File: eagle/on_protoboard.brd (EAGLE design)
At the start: 100 x 80 mm, 15 parts, among them IC2 7812T, K1 G6AK-434P

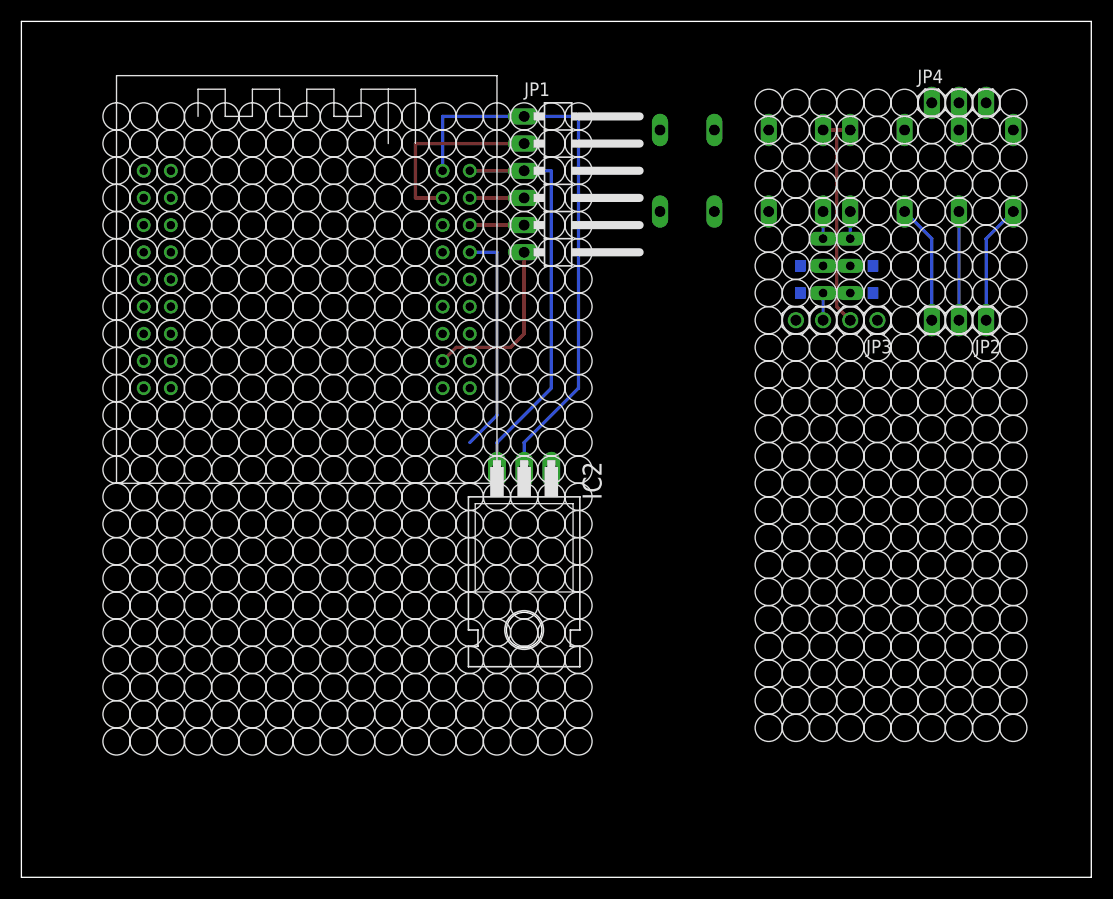
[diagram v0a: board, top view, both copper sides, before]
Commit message: Add digital pulse output device
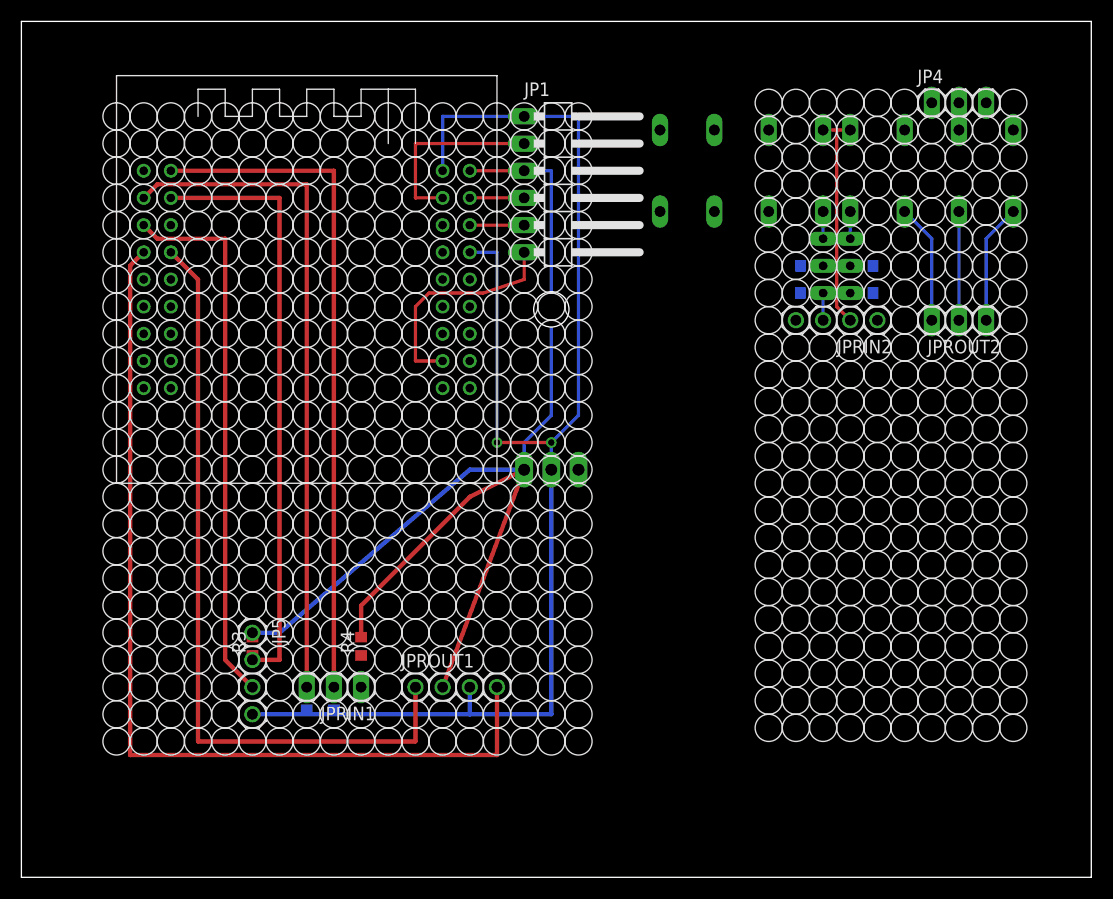
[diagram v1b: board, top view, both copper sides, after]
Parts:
- added JP5, JPROUT1: (no value), pinhead:1X04
- added JPRIN1: (no value), pinhead:1X03
- added R1, R2, R3, R4: 10k, rcl:R0603
- RR1, RS1: value (none) -> 1k
- RR2, RS2: value (none) -> 10k
- moved IC2 20.5 mm to (49.5, 48.3), flipped to the bottom, turned to 0 degrees
- renumbered JP2 to JPROUT2, JP3 to JPRIN2
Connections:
- net N$12 renamed SET_STATE_OUT
- net N$13 renamed RESET_STATE_OUT
- net N$14 renamed SET_IN
- net N$17 renamed RESET_IN
- new net N$18: ESP-32S-ADAPTER-PCB1.IO35, JPRIN1.3, R1.2
- new net N$20: ESP-32S-ADAPTER-PCB1.IO36, JPRIN1.2, R2.2
- new net N$22: JPRIN1.1, R4.1
- new net N$23: ESP-32S-ADAPTER-PCB1.IO25, JPROUT1.1
- new net N$24: ESP-32S-ADAPTER-PCB1.IO26, JPROUT1.4
- new net U1RXD: ESP-32S-ADAPTER-PCB1.IO34, JP5.2, R3.1
- new net U1TXD: ESP-32S-ADAPTER-PCB1.IO33, JP5.3
- net +3V3: now also JP5.1, JPROUT1.2, R3.2, R4.2
- net GND: now also JP5.4, JPROUT1.3, R1.1, R2.1
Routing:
- net N$24: track 0.00 -> 88.2 mm
- net N$23: track 0.00 -> 72.2 mm
- net +3V3: track 42.7 -> 112.4 mm
- net N$20: track 0.00 -> 63.5 mm
- net N$18: track 0.00 -> 62.8 mm
- net GND: track 74.3 -> 130.6 mm, vias 0 -> 2
- net U1RXD: track 0.00 -> 55.9 mm
- net U1TXD: track 0.00 -> 51.1 mm
- net N$6: track 16.3 -> 21.1 mm

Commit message: fix rf433
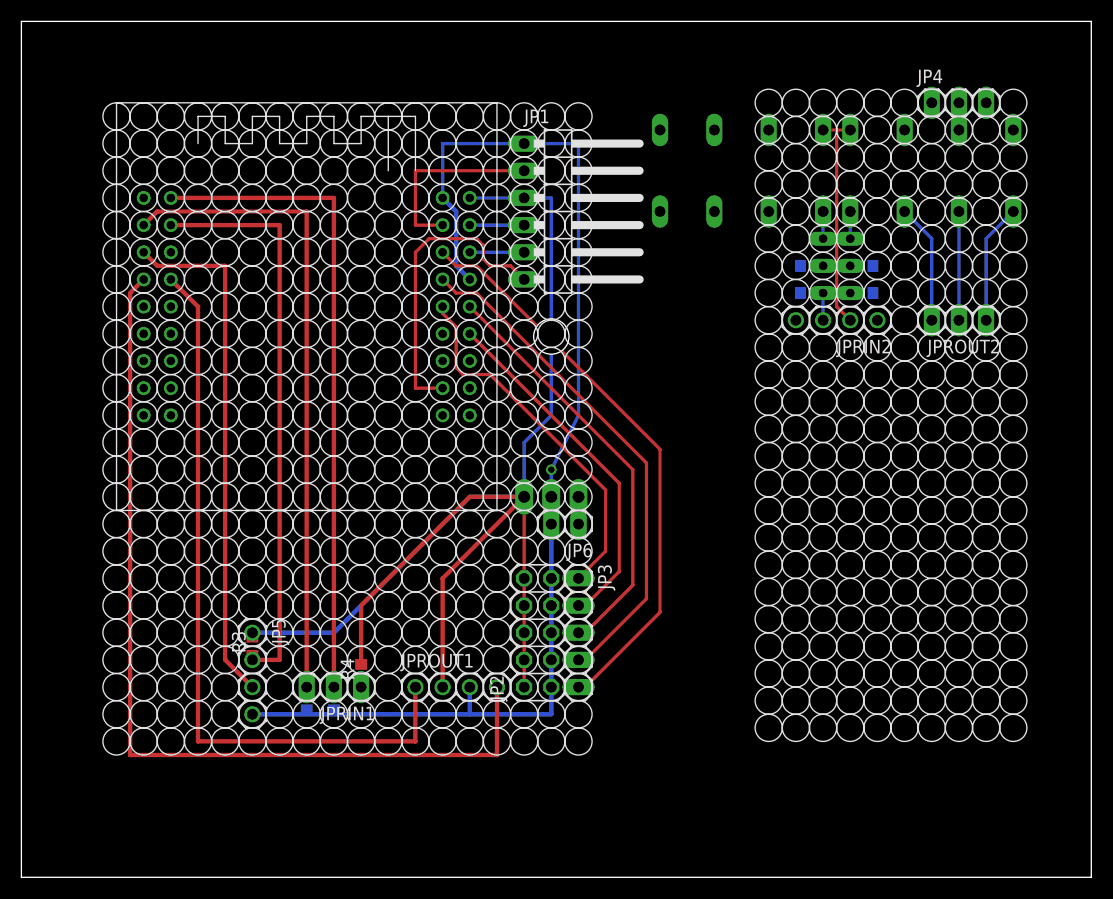
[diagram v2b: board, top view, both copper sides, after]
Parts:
- added JP2: (no value), pinhead:2X05
- added JP3: (no value), pinhead:1X05
- added JP6: (no value), pinhead:1X02
- moved ESP-32S-ADAPTER-PCB1 2.54 mm to (26.7, 53.3)
- moved IC2 2.54 mm to (49.5, 45.7)
- moved JP1 2.54 mm to (50.8, 62.2)
- moved R4 2.54 mm to (31.8, 19.1)
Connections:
- new net N$12: ESP-32S-ADAPTER-PCB1.IO19, JP3.1
- new net N$13: ESP-32S-ADAPTER-PCB1.IO18, JP3.2
- new net N$14: ESP-32S-ADAPTER-PCB1.IO21, JP3.3
- new net N$17: ESP-32S-ADAPTER-PCB1.IO22, JP3.4
- new net N$21: ESP-32S-ADAPTER-PCB1.IO23, JP3.5
- net +3V3: now also JP2.10, JP2.2, JP2.4, JP2.6, JP2.8
- net +5V: now also JP6.1
- net GND: now also JP2.1, JP2.3, JP2.5, JP2.7, JP2.9, JP6.2
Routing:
- net N$21: track 0.00 -> 53.7 mm
- net N$17: track 0.00 -> 47.6 mm
- net N$14: track 0.00 -> 39.3 mm
- net N$12: track 0.00 -> 34.3 mm
- net N$13: track 0.00 -> 33.1 mm
- net GND: track 130.6 -> 110.9 mm, vias 2 -> 1
- net +3V3: track 112.4 -> 130.9 mm
- net N$6: track 21.1 -> 28.2 mm
- net N$24: track 88.2 -> 85.6 mm
- net N$23: track 72.2 -> 69.6 mm
- net N$20: track 63.5 -> 61.0 mm
- net U1TXD: track 51.1 -> 48.6 mm
- net U1RXD: track 55.9 -> 53.3 mm
- net N$18: track 62.8 -> 60.2 mm
